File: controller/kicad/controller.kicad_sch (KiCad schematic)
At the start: 34 parts, among them J1 pcie_98, J2 USB_C_Receptacle_USB2.0, SW1 SW_MEC_5E, U1 WeAct_STM32H750_Module, U10 ESD5344D, U11 ESD5344D, U12 ESD5344D, U13 ESD5344D, U14 ESD5344D, U15 ESD5344D, U16 CP2102N-A01-GQFN28-Interface_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, U2 ESD5344D, U3 ESD5344D, U4 ESD5344D, U5 ESD5344D, U6 ESD5344D, U7 ESD5344D, U8 ESD5344D, U9 ESD5344D

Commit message: Added a comment to the Controller's schematic.
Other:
- note added: "MCU Module modifications: * Remove diode D10. This is the diode adjacent to the red LED near the USB connector."
- note added: "TODO: Run the auxilary USB port from the 5V of the bus power rather than the USB power."
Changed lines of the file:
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@@
     (effects (font (size 3 3) (thickness 0.6) bold) (justify left bottom))
+  )
+  (text "TODO: Run the auxilary USB port from the 5V of\nthe bus power rather than the USB power."
+    (at 140.335 180.975 0)
+    (effects (font (size 2.54 2.54) (thickness 0.508) bold (color 255 0 0 1)) (justify left bottom))
   )
   (text "TODO: Extend the pads of electrolitic caps and protection diodes"
@@
     (effects (font (size 3 3) (thickness 0.6) bold) (justify left bottom))
   )
+  (text "MCU Module modifications:\n* Remove diode D10. This is the diode adjacent\n  to the red LED near the USB connector."
+    (at 134.62 45.085 0)
+    (effects (font (size 2.54 2.54)) (justify left bottom))
+  )
   (text "TODO: route reset switch at card edge" (at 139.065 159.385 0)

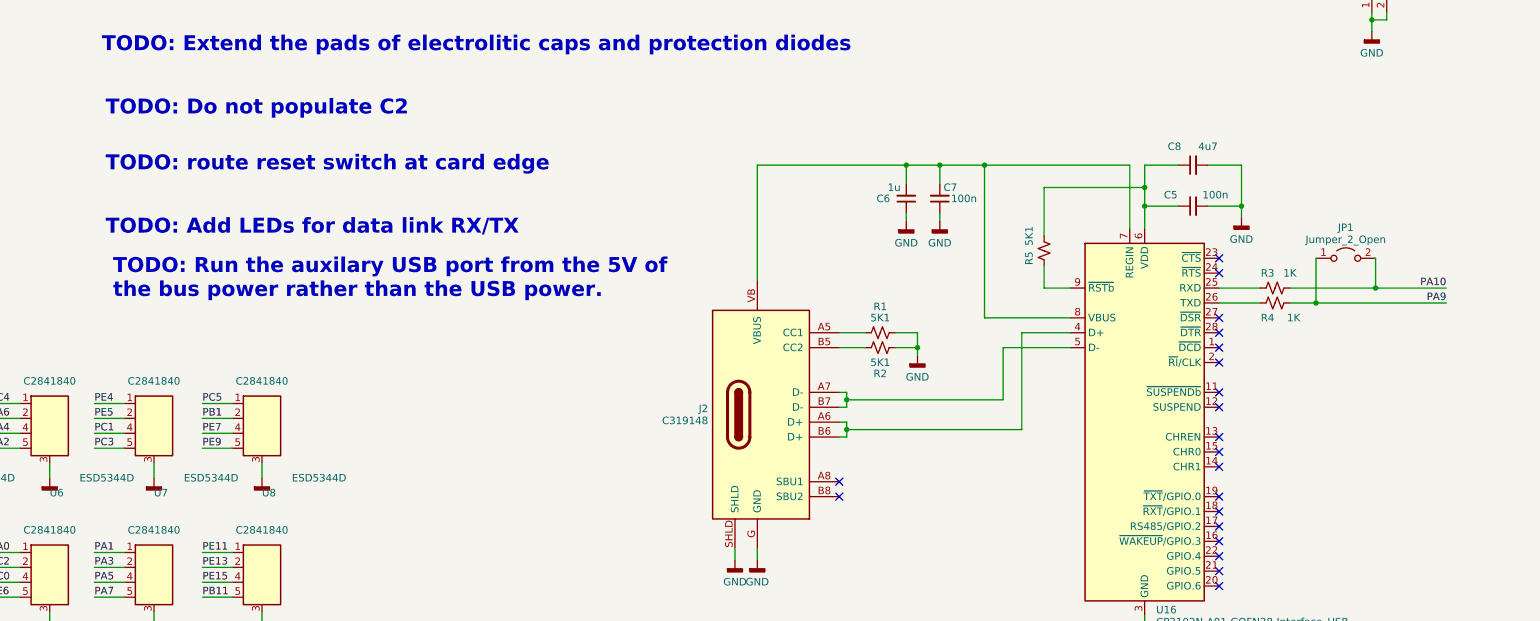
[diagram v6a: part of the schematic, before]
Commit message: Updated controller serial port schematic. Now powered by bus and has TX/RX leds.
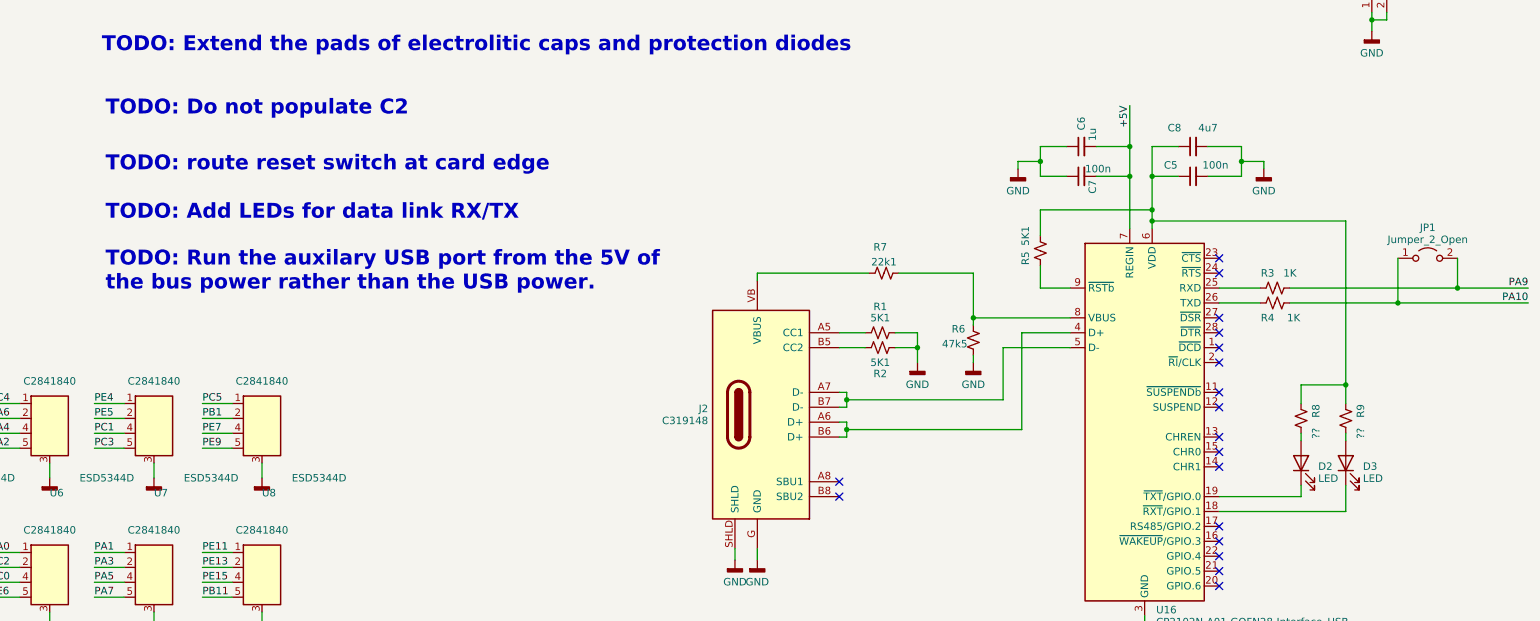
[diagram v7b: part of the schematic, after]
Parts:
- added D2, D3: LED, symbol Device:LED
- added R6: 47k5, Resistor_SMD:R_0603_1608Metric, symbol Device:R_Small_US
- added R7: 22k1, Resistor_SMD:R_0603_1608Metric, symbol Device:R_Small_US
- added R8, R9: ??, Resistor_SMD:R_0603_1608Metric, symbol Device:R_Small_US
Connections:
- net +5V: now also C6.2, C7.2, U16.7 (REGIN)
- net GND: now also R6.1
- net PA10: now also JP1.1 (A), R4.2; no longer JP1.2 (B), R3.2
- net PA9: now also JP1.2 (B), R3.2; no longer JP1.1 (A), R4.2
- net at C5.1, C8.1, R5.2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: now also R8.1, R9.1
- net at U16.18 (~{RXT}/GPIO.1): now also D3.1 (K)
- net at U16.19 (~{TXT}/GPIO.0): now also D2.1 (K)
- new net: D2.2 (A), R8.2
- new net: J2.VB (VBUS), R7.2
- new net: R6.2, R7.1, U16.8 (VBUS)
- new net: D3.2 (A), R9.2
- no-connect marks 80 -> 78
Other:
- moved on the sheet: C5, C6, C7, C8, JP1, R5

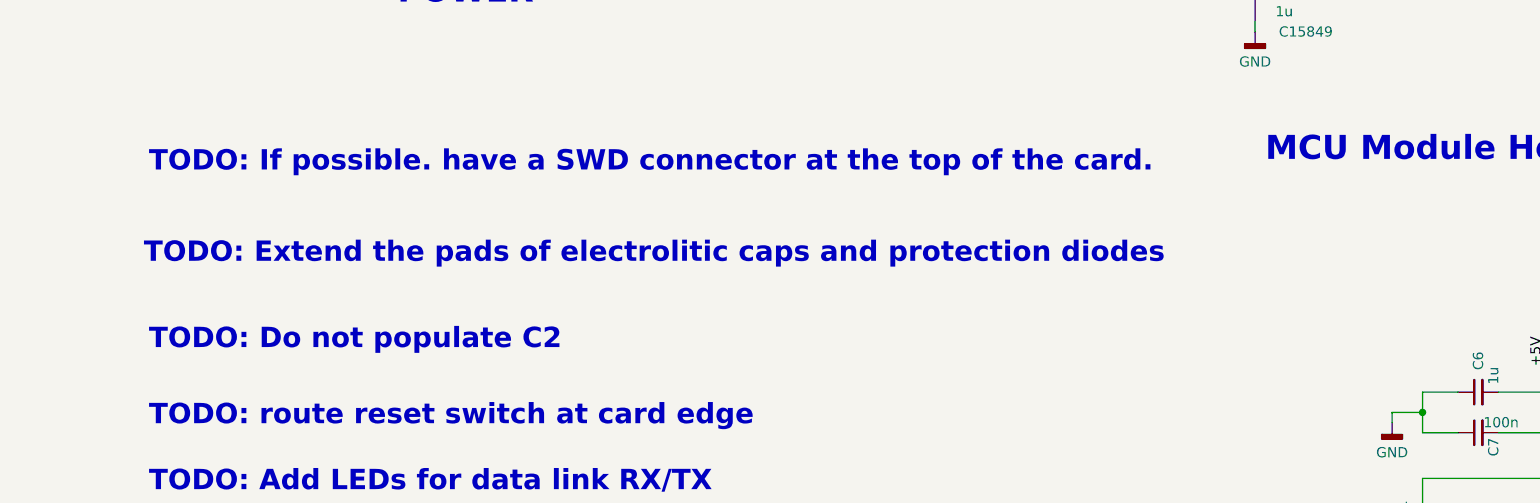
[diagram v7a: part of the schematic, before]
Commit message: Updated controller and power supply schematics.
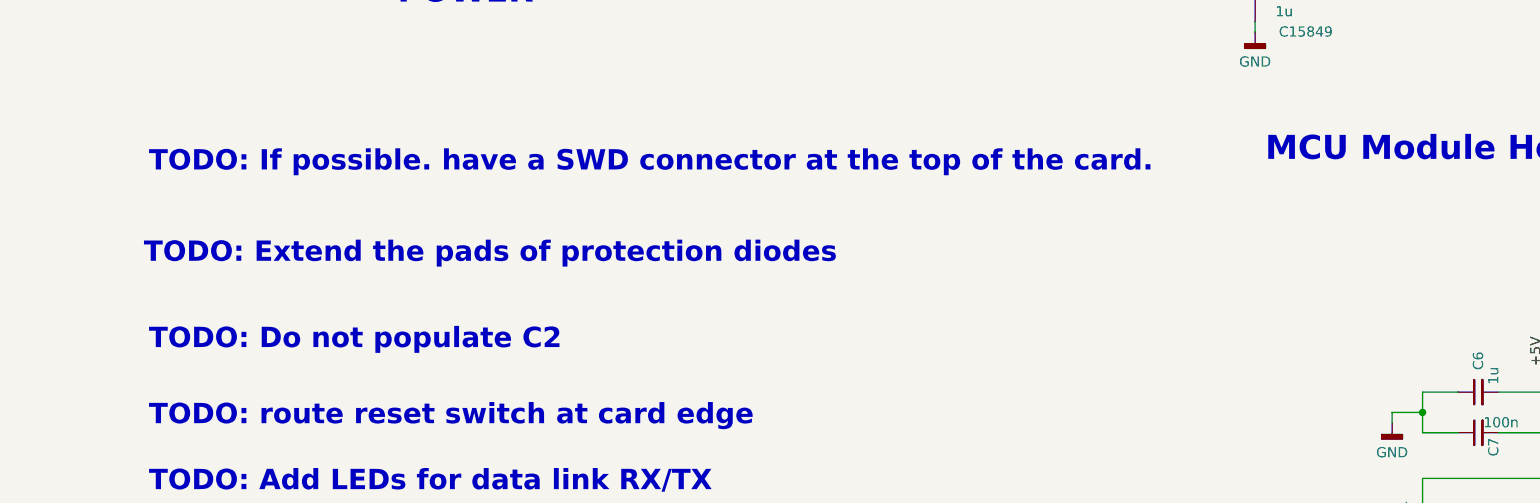
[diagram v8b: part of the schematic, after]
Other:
- note added: "TODO: Extend the pads of protection diodes"
- note removed: "TODO: Extend the pads of electrolitic caps and protection diodes"
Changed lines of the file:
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@@
     (effects (font (size 2.54 2.54) (thickness 0.508) bold (color 255 0 0 1)) (justify left bottom))
   )
-  (text "TODO: Extend the pads of electrolitic caps and protection diodes"
-    (at 138.43 139.065 0)
+  (text "TODO: Extend the pads of protection diodes" (at 138.43 139.065 0)
     (effects (font (size 2.54 2.54) (thickness 0.508) bold (color 255 0 0 1)) (justify left bottom))
   )
